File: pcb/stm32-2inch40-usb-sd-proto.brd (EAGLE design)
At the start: 99.1 x 97.8 mm, 126 parts, among them IC1 CAT24M01WI-GT3, IC2 STM32F103RBT6, IC4 MAX487-S, K1 ZF112, K2 ZF112, Q1 32768Hz, Q2 8MHz, Q3 MMBT2222, Q4 MMBT2222, Q6 MMBT2222, SW1 KSS-2EG4430, SW2 KSS-2EG4430, SW3 KSS-2EG4430, SW4 KSS-2EG4430, SW5 KSS-2EG4430, U1 L1117-3.3, U2 L1117-3.3, X1 MCV3, X2 MKDSN1,5/2-5,08, X3 MKDSN1,5/6-5,08

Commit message: production ready, small fixes
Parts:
- C10, C11: value 0.1 -> 22pF
- C15, C16: device rc-master-smd:C0805 -> rc-master-smd:C0603
- C18: value 47pF -> 0.1
- C19: value 47pF -> 0.1; device rc-master-smd:C0603 -> rc-master-smd:C0805
- C20, C27: value 10uF -> 0.1
- C24: value 0.1 -> 10uF; device rc-master-smd:C0603 -> rc-master-smd:C0805
- C25: value 0.1 -> 10uF
- C3: value 0.1 -> 47pF
- C4: value 10pF -> 47pF
- C5: value 10pF -> 0.1
- C6, C7: value 22pF -> 0.1
- C8, C9: value 0.1 -> 10pF
- D1: value PESD1CAN -> (none); device protect:SOT23 -> semicon-smd-ipc:SOD87
- D2: value (none) -> PESD1CAN; device semicon-smd-ipc:SOD87 -> protect:SOT23
- IC3: value (none) -> MAX487-S; device esp-modules:ESP12 -> rs232-rs485:SO08
- IC4: value MAX487-S -> (none); device rs232-rs485:SO08 -> esp-modules:ESP12
- L1: value bead -> FB_0603
- L2: value FB_0603 -> bead
- Q1: value 32768Hz -> (none); device crystal:TC38H-G -> semiconductor:SOT23
- Q2: value 8MHz -> 32768Hz; device discrete:HC49/S -> crystal:TC38H-G
- Q3: value MMBT2222 -> 8MHz; device semiconductor:SOT23 -> discrete:HC49/S
- Q5: value (none) -> MMBT2222
- R10: value 2.2K -> 4.7K
- R12: value 1K -> 1.5K
- R13: value 2K -> 220
- R14: value 3.9K -> 220
- R15: value 1M -> 10K
- R16: value 2K -> 10K
- R17: value 200 -> 2.2K
- R18: value 200 -> 10K
- R19: value 200 -> 1K
- R20: value 4.7K -> 2K
- R21: value 10 -> 3.9K
- R22: value 2K -> 1M
- R23: value 10K -> 2K
- R24: value 10K -> 200; device rc-master-smd:R0805 -> rc-master-smd:R0603
- R25, R26: value 10 -> 200
- R27: value 10 -> 4.7K
- R29: value 10 -> 2K
- R3, R4: value 4.7K -> 10K
- R30, R52: value 10 -> 10K
- R41, R43, R45: value 10K -> 10
- R42: value 1.5K -> 10
- R44, R46: value 560 -> 10
- R48: value 10K -> 560
- R49: value 22 -> 560
- R5, R6: value 220 -> 22
- R50: value 22 -> 10; device rc-master-smd:R0603 -> rc-master-smd:R0805
- R53, R54: value 10K -> 1K
- R55, R56: value 1K -> 10K
- R8: value 10K -> 4.7K
- moved R50 76.3 mm to (7.62, 70.5), flipped to the bottom, turned to 270 degrees
- moved Q4 67.0 mm to (46.4, 12.1), turned to 90 degrees
- moved IC3 65.0 mm to (48.9, 28.6), flipped to the bottom, turned to 90 degrees
- moved IC4 65.0 mm to (7.62, 78.7), flipped to the top, turned to 0 degrees
- moved C3 59.3 mm to (58.4, 11.9), flipped to the top
- moved Q5 56.0 mm to (62.2, 78.1), turned to 0 degrees
- moved R25 54.0 mm to (26.0, 49.5)
- moved C24 52.1 mm to (62.2, 69.2), turned to 180 degrees
- moved R6 52.0 mm to (58.4, 13.5)
- moved R5 51.9 mm to (58.4, 15.1)
- moved R12 50.8 mm to (58.4, 18.3), turned to 0 degrees
- moved C7 49.7 mm to (14.1, 49.2), flipped to the top, turned to 0 degrees
- moved R26 49.5 mm to (26.0, 46.4)
- moved C19 49.2 mm to (10.2, 6.99), flipped to the bottom, turned to 180 degrees
- moved C6 48.7 mm to (9.53, 45.4)
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- renumbered ESBOOT to SW7, ESRST to SW6, STAMP to STMP1, U$1 to LOGO1
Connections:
- net !LCD_CS: now also R26.2, R27.1; no longer R19.2, R20.1
- net !RESET: now also C6.1, R18.1; no longer C3.1, R11.1
- net !SD_CS: now also R3.1; no longer R43.1
- net !SD_DET: now also R4.1; no longer R45.1
- net +3V3: now also C14.1, C17.1, C20.1, Q1.2, R10.2, R13.1, R18.2, R27.2, R28.2, R30.2, R8.2; no longer C10.1, C8.1, C9.1, Q5.2, R11.2, R20.2, R21.2, R23.2, R3.2, R4.2, R5.1
- net +5V: now also C18.1, C19.1, D1.1, IC3.8, R49.2; no longer C14.1, C15.1, D2.1, IC4.8, R46.2
- net +5V1: now also C24.1; no longer C27.1
- net BOOT0: now also R15.1; no longer R8.1
- net BOOT1: now also R14.1, R16.1; no longer R6.1, R9.1
- net DE3: now also IC3.4; no longer IC4.4
- net ES_3V3: now also C27.1, IC4.8, R50.1; no longer C20.1, IC3.8, R52.1
- net ES_ADC: now also IC4.2; no longer IC3.2
- net ES_CHEN: now also IC4.3, R50.2; no longer IC3.3, R52.2
- net ES_GND: now also C24.2, IC4.9, Q5.2, R52.1, R55.1, R56.1; no longer C20.2, IC3.9, Q4.2, R24.1, R53.1, R54.1
- net ES_GPIO0: now also IC4.12; no longer IC3.12
- net ES_GPIO12: now also IC4.6; no longer IC3.6
- net ES_GPIO13: now also IC4.7; no longer IC3.7
- net ES_GPIO14: now also IC4.5; no longer IC3.5
- net ES_GPIO15: now also IC4.10, R52.2; no longer IC3.10, R24.2
- net ES_GPIO16: now also IC4.4; no longer IC3.4
- net ES_GPIO2: now also IC4.11; no longer IC3.11
- net ES_GPIO4: now also IC4.14; no longer IC3.14
- net ES_GPIO5: now also IC4.13; no longer IC3.13
- net ES_K1: now also R53.1; no longer R55.1
- net ES_K2: now also R54.1; no longer R56.1
- net ES_RST: now also IC4.1; no longer IC3.1
- net ES_RXD: now also IC4.15; no longer IC3.15
- net ES_TXD: now also IC4.16; no longer IC3.16
- net GND: now also C20.2, D2.3, IC3.5, Q2.GND, Q4.2, R16.2, R17.1, R23.1, R47.1, R48.1; no longer C7.2, D1.3, IC4.5, Q1.GND, Q3.2, R10.1, R16.1, R41.1, R44.1, R9.2
- net LCD_CLK: now also R25.2; no longer R18.2
- net LCD_DATA: now also R24.2; no longer R17.2
- net N$1: now also Q1.3, R12.2; no longer Q5.3, R42.2
- net N$10: now also R5.1; no longer R49.1
- net N$11: now also R39.1; no longer R33.1
- net N$13: now also R13.2; no longer R5.2
- net N$14: now also R40.1; no longer R34.1
- net N$15: now also R31.1; no longer R25.1
- net N$16: now also R32.1; no longer R26.1
- net N$17: now also R33.1; no longer R27.1
- net N$18: now also R34.1; no longer R28.1
- net N$19: now also R35.1; no longer R29.1
- net N$2: now also D1.2; no longer D2.2
- net N$20: now also R36.1; no longer R30.1
- net N$21: now also R37.1; no longer R31.1
- net N$22: now also R38.1; no longer R32.1
- net N$23: now also R41.1; no longer R35.1
- net N$24: now also R42.1; no longer R36.1
- net N$25: now also R43.1; no longer R37.1
- net N$26: now also R44.1; no longer R38.1
- net N$27: now also R45.1; no longer R39.1
- net N$28: now also R46.1; no longer R40.1
- net N$29: now also Q4.3; no longer Q3.3
- net N$3: now also R15.2, R17.2; no longer R10.2, R8.2
- net N$30: now also R14.2; no longer R6.2
- net N$31: now also R28.1; no longer R21.1
- net N$32: now also Q4.1, R29.1; no longer Q3.1, R22.1
- net N$33: now also R19.1; no longer R12.1
- net N$34: now also R20.1; no longer R13.1
- net N$35: now also R21.1; no longer R14.1
- net N$36: now also R6.1; no longer R50.1
- net N$37: now also Q6.1, R54.2; no longer Q4.1, R53.2
- net N$38: now also Q1.1; no longer Q5.1
- net N$41: now also Q6.3; no longer Q4.3
- net N$42: now also Q5.3; no longer Q6.3
- net N$44: now also D2.1, IC3.6, R49.1; no longer D1.1, IC4.6, R46.1
- net N$46: now also Q5.1, R53.2; no longer Q6.1, R54.2
- net N$6: now also D2.2, IC3.7, R48.2; no longer D1.2, IC4.7, R44.2
- net N$7: now also C5.1, L1.2, R11.2, R3.2, R4.2, R9.2; no longer C17.1, L2.2, R43.2, R45.2, R47.2, R48.2
- net N$8: now also R11.1; no longer R48.1
- net N$9: now also R9.1; no longer R47.1
- net OSC32_IN: now also C8.1, Q2.2; no longer C4.1, Q1.2
- net OSC32_OUT: now also C9.1, Q2.1; no longer C5.1, Q1.1
- net OSC_IN: now also C10.1, Q3.1, R22.2; no longer C6.1, Q2.1, R15.2
- net OSC_OUT: now also C11.1, Q3.2, R22.1; no longer C7.1, Q2.2, R15.1
- net PA0: now also C7.2, R19.2, R20.2, R21.2, R23.2; no longer C24.2, R12.2, R13.2, R14.2, R16.2
- net PA1: now also R26.1; no longer R19.1
- net PA2: now also R24.1; no longer R17.1
- net PA4: now also R25.1; no longer R18.1
- net PB0: now also R45.2; no longer R39.2
- net PB1: now also R46.2; no longer R40.2
- net PB4: now also R29.2; no longer R22.2
- net PC0: now also R39.2; no longer R33.2
- net PC1: now also R40.2; no longer R34.2
- net PC2: now also R41.2; no longer R35.2
- net PC3: now also R42.2; no longer R36.2
- net PC4: now also R43.2; no longer R37.2
- net PC5: now also R44.2; no longer R38.2
- net RXD1: now also R30.1; no longer R23.1
- net RXD3: now also IC3.1; no longer IC4.1
- net SCL2: now also R8.1; no longer R3.1
- net SDA2: now also R10.1; no longer R4.1
- net TIM3_CH1: now also R31.2; no longer R25.2
- net TIM3_CH2: now also R32.2; no longer R26.2
- net TIM3_CH3: now also R33.2; no longer R27.2
- net TIM3_CH4: now also R34.2; no longer R28.2
- net TIM4_CH1: now also R35.2; no longer R29.2
- net TIM4_CH2: now also R36.2; no longer R30.2
- net TIM4_CH3: now also R37.2; no longer R31.2
- net TIM4_CH4: now also R38.2; no longer R32.2
- net TXD3: now also IC3.2, IC3.3, R47.2; no longer IC4.2, IC4.3, R41.2
- net USB_DM: now also C3.1, R6.2; no longer C18.1, R50.2
- net USB_DP: now also C4.1, R12.1, R5.2; no longer C19.1, R42.1, R49.2
- net VDDA: now also C15.1, C7.1, L2.2; no longer C11.1, C24.1, L1.2

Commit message: production ready, small fixes
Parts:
- moved C19 1.90 mm to (12.1, 6.99)
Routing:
- net +3V3: track 230.8 -> 228.8 mm
- net PA0: track 54.1 -> 53.1 mm
- net PA1: track 58.2 -> 57.3 mm
- net !RESET: track 89.5 -> 88.6 mm
- net +5V: track 101.6 -> 100.7 mm
- net PA2: track 52.2 -> 51.3 mm
- net PB4: track 23.0 -> 22.2 mm
- net PA3: track 39.2 -> 38.4 mm
- net RS485_A: track 8.96 -> 8.21 mm
- net PA4: track 46.6 -> 45.9 mm
- net PC13: track 62.8 -> 62.2 mm
- net RS485_B: track 7.37 -> 6.81 mm
- net PA5: track 41.3 -> 40.8 mm

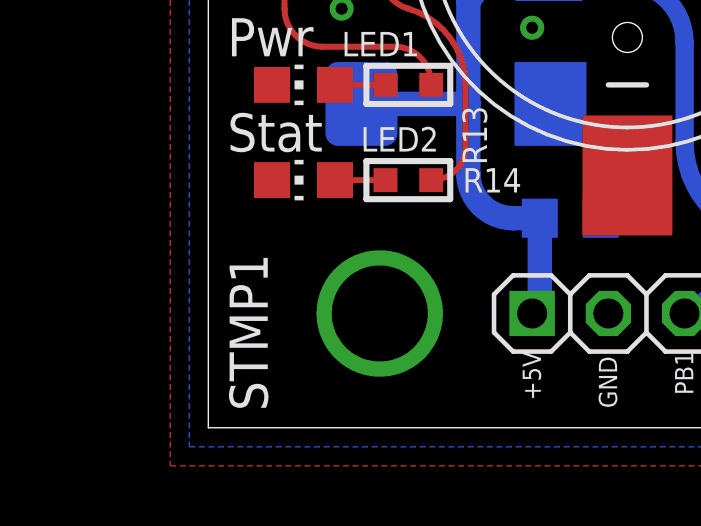
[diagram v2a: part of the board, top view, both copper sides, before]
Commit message: change link on silk layer
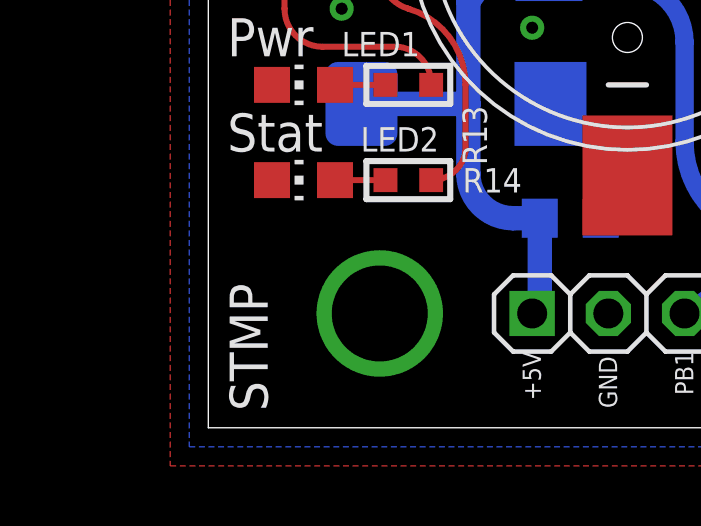
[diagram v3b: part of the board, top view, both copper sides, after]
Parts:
- renumbered STMP1 to STMP
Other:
- board text added: "tuxotronic.org/stm32stamp2i"
- board text removed: "tuxotronic.org"
